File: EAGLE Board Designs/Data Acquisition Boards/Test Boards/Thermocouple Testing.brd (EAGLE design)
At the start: 78.4 x 61 mm, 25 parts, among them U1 MAX31855K, U2 MAX31855K, U3 MAX31855K, X1 CONNECTOR-4NANO-FIT-VERTICAL-4

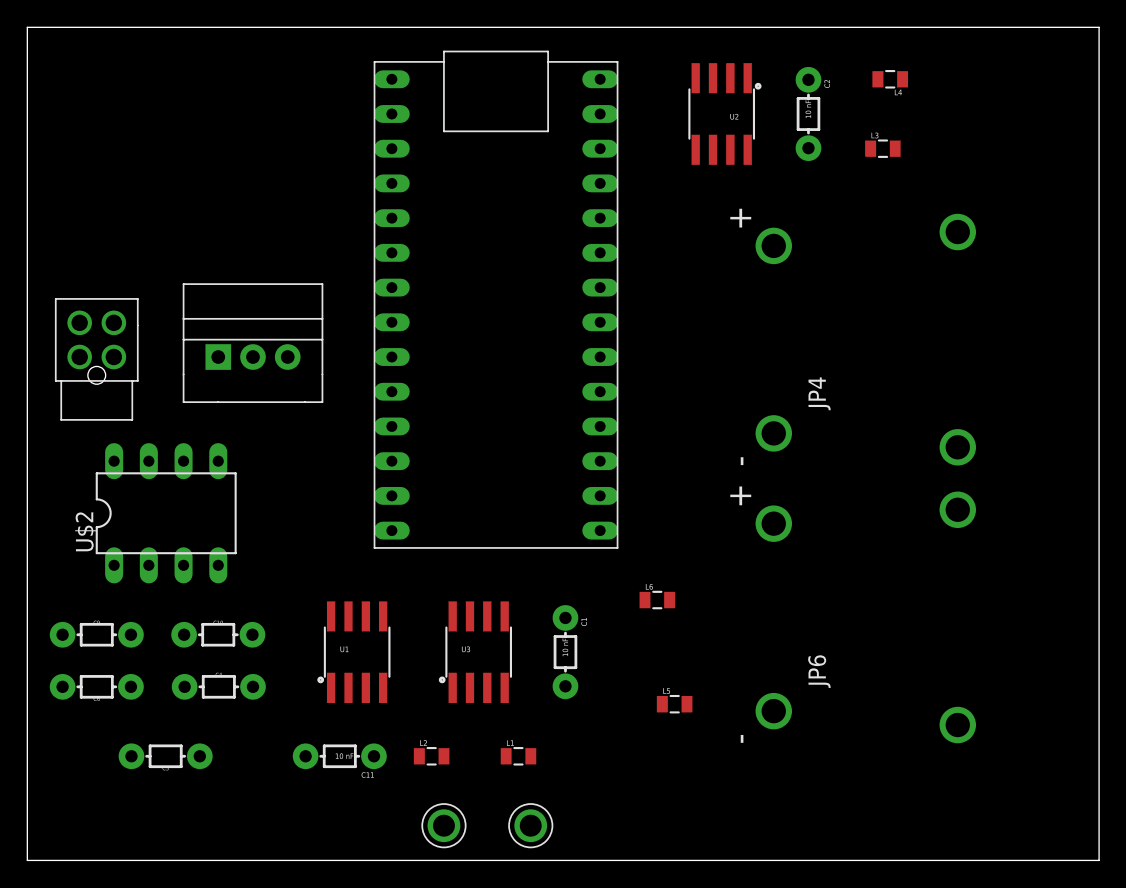
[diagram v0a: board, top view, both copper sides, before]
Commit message: Routed thermocouple test board
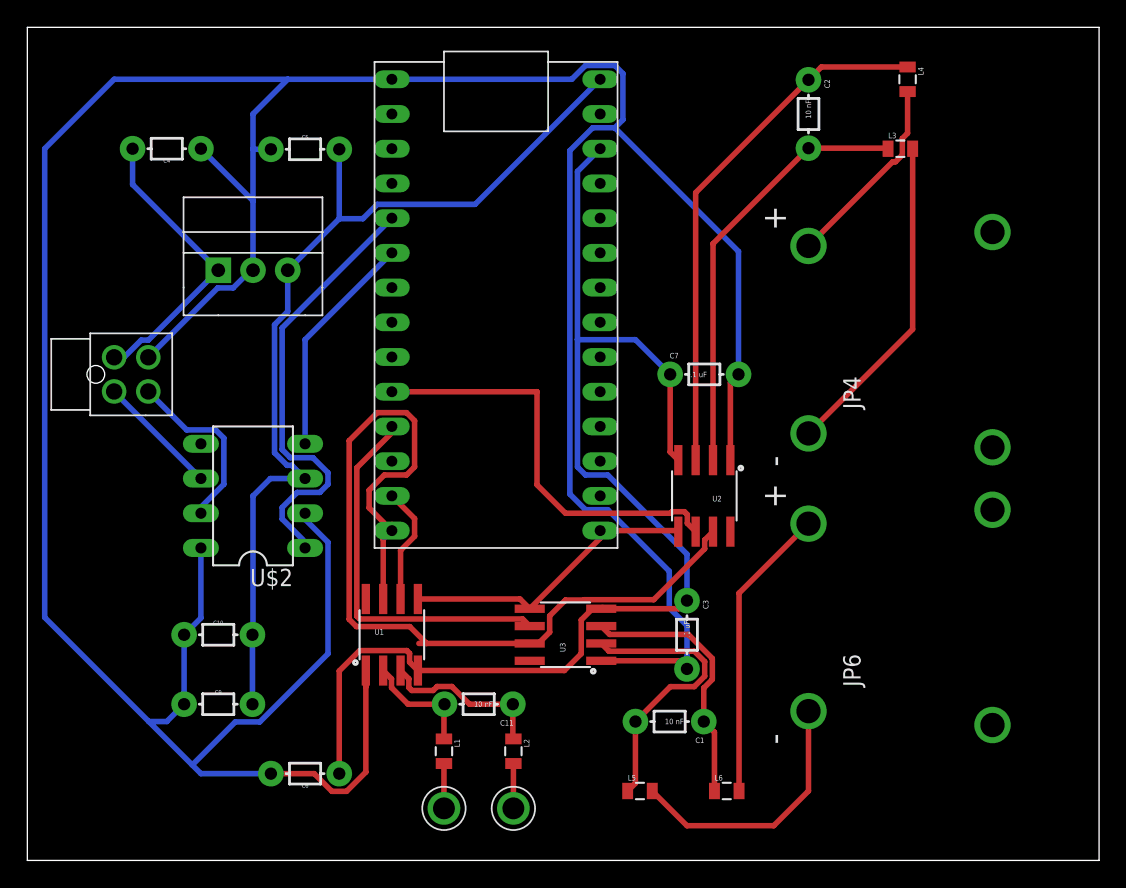
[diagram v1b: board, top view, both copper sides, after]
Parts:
- added C3, C7: .1 uF, HyTechDevices:AXIAL-5MM
- moved C5 45.6 mm to (20.3, 52.0), turned to 0 degrees
- moved C4 39.6 mm to (10.2, 52.1), turned to 180 degrees
- moved U2 28.0 mm to (49.5, 26.7)
- moved C6 16.5 mm to (20.3, 6.35)
- moved L6 14.9 mm to (51.2, 5.08)
- moved C11 10.9 mm to (33.0, 11.4)
- moved C9 10.2 mm to (14.0, 11.4)
- moved C1 9.16 mm to (47.0, 10.2), turned to 180 degrees
- moved L5 6.84 mm to (44.8, 5.08)
- moved U$2 6.48 mm to (16.5, 26.7), turned to 90 degrees
- moved U$3 6.48 mm to (30.5, 3.81)
- moved U3 6.48 mm to (39.4, 16.5), turned to 90 degrees
- moved REG 6.35 mm to (16.5, 43.2)
- moved L2 5.99 mm to (35.6, 7.99), turned to 270 degrees
- moved L1 5.46 mm to (30.5, 7.99), turned to 270 degrees
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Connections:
- net +12V: now also X1.P$1; no longer X1.P$4
- net 3.3V: now also C3.P$1, C7.P$1
- net CANH: now also X1.P$4; no longer X1.P$3
- net GND: now also C3.P$2, C7.P$2, X1.P$3; no longer X1.P$1
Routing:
- net GND: track 0.00 -> 274.2 mm
- net 3.3V: track 0.00 -> 92.0 mm
- net 5V: track 0.00 -> 70.1 mm
- net MISO: track 0.00 -> 68.2 mm
- net N$6: track 0.00 -> 38.9 mm
- net N$16: track 0.00 -> 32.9 mm
- net N$12: track 0.00 -> 31.6 mm
- net N$11: track 0.00 -> 30.9 mm
- net N$10: track 0.00 -> 27.9 mm
- net N$13: track 0.00 -> 24.0 mm
- net SCK: track 0.00 -> 22.1 mm
- net +12V: track 0.00 -> 21.7 mm
- net N$21: track 0.00 -> 21.7 mm
- net N$19: track 0.00 -> 20.9 mm
- net N$15: track 0.00 -> 19.4 mm
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
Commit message: Made smd version of wheel speed sensor and updated thermocouple testing board
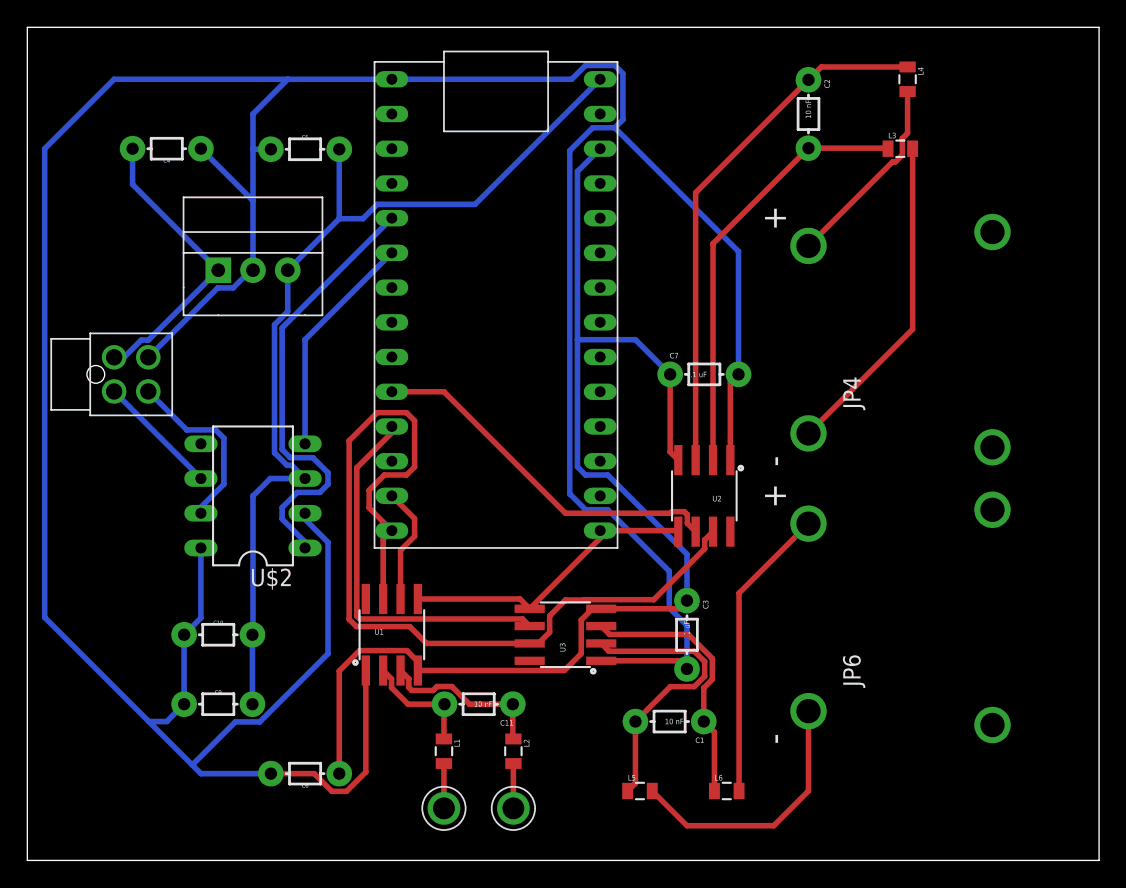
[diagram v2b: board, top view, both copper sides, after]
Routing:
- net N$11: track 30.9 -> 26.9 mm
- net 3.3V: track 92.0 -> 90.5 mm
- net GND: track 274.2 -> 272.9 mm
- net MISO: track 68.2 -> 67.2 mm
- net N$7: track 13.1 -> 12.4 mm
